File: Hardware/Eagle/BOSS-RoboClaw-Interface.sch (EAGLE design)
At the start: 9 parts, among them IC1 ISO7221ISO7221, J1 MOLEX 22112022, J2 MOLEX 22122034, J3 Amphenol 75869-130LF, J4 SAMTEC ESQ-105-44-G-S, J5 SAMTEC ESW-110-44-S-D, X1 Amphenol L77SDAH15SOL2RM8C309

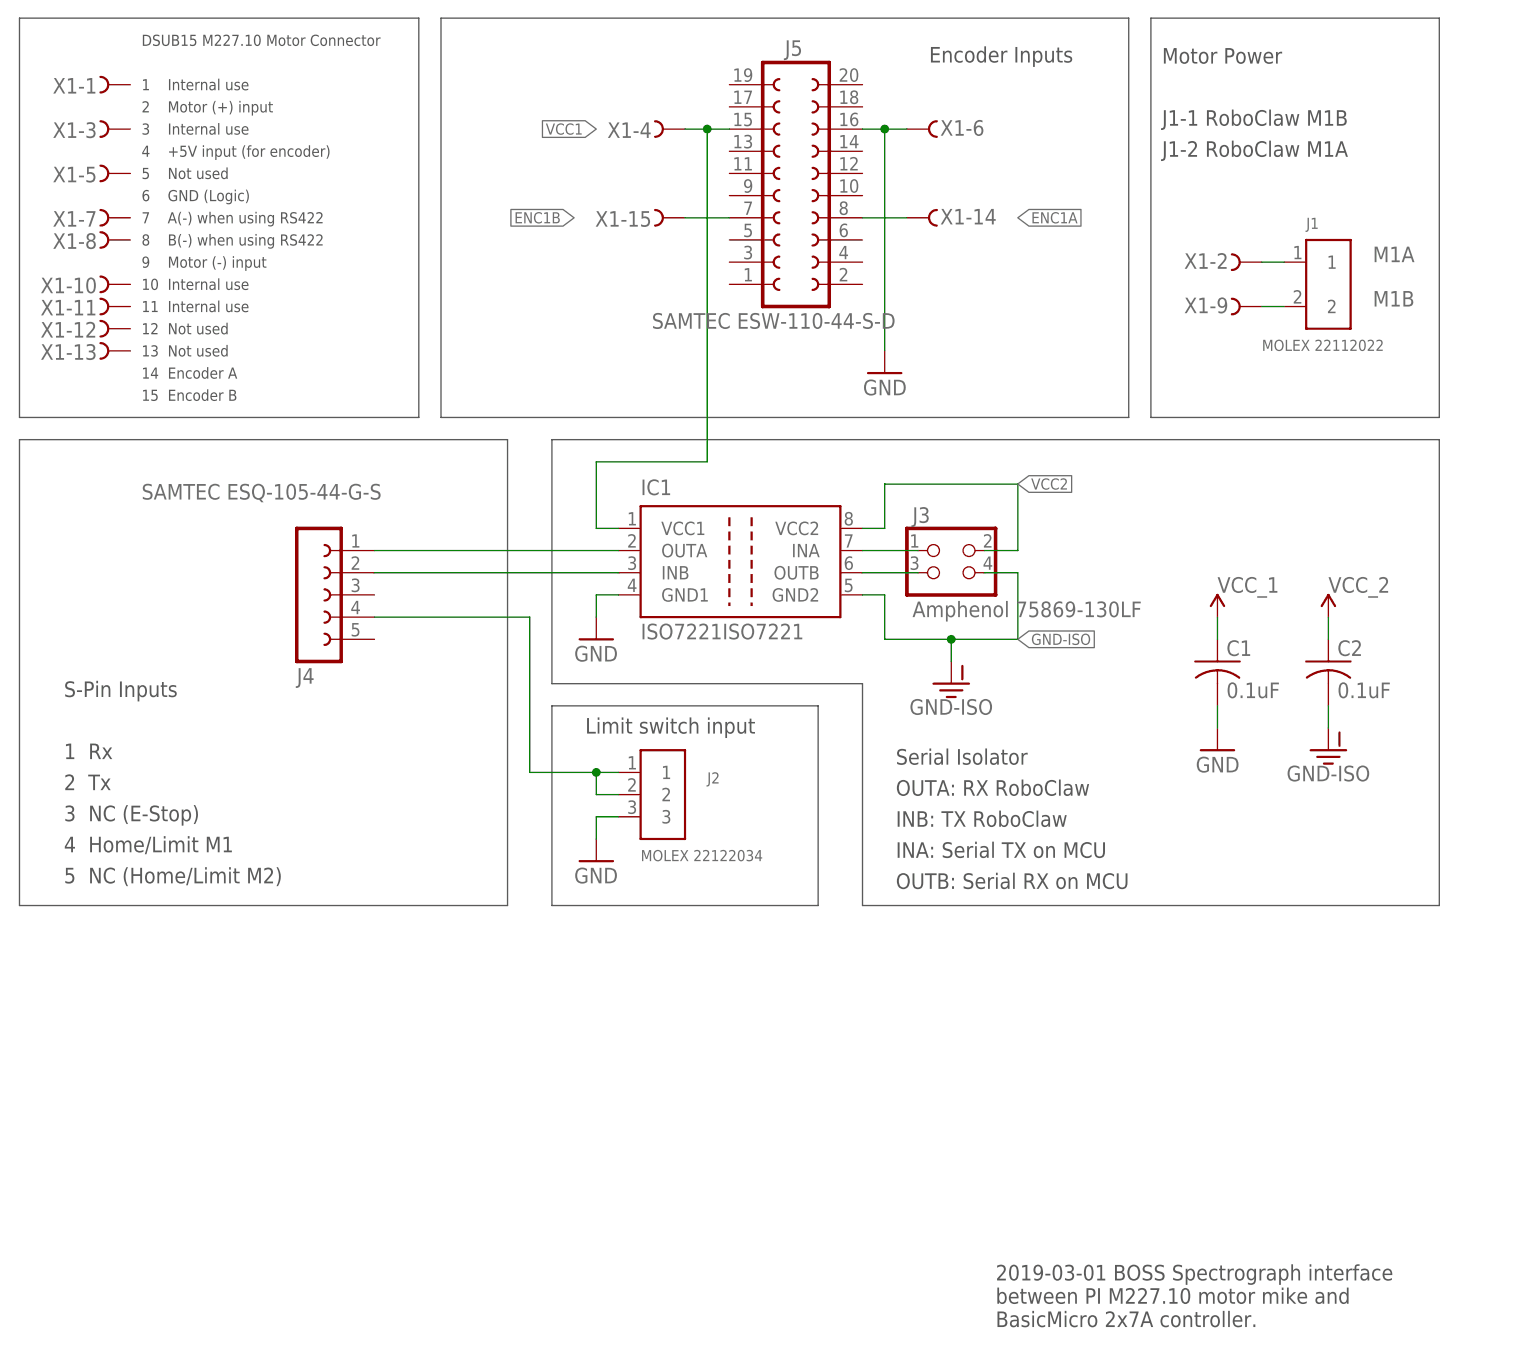
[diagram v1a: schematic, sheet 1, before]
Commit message: New headers for RoboClaw interface (need to check connections)
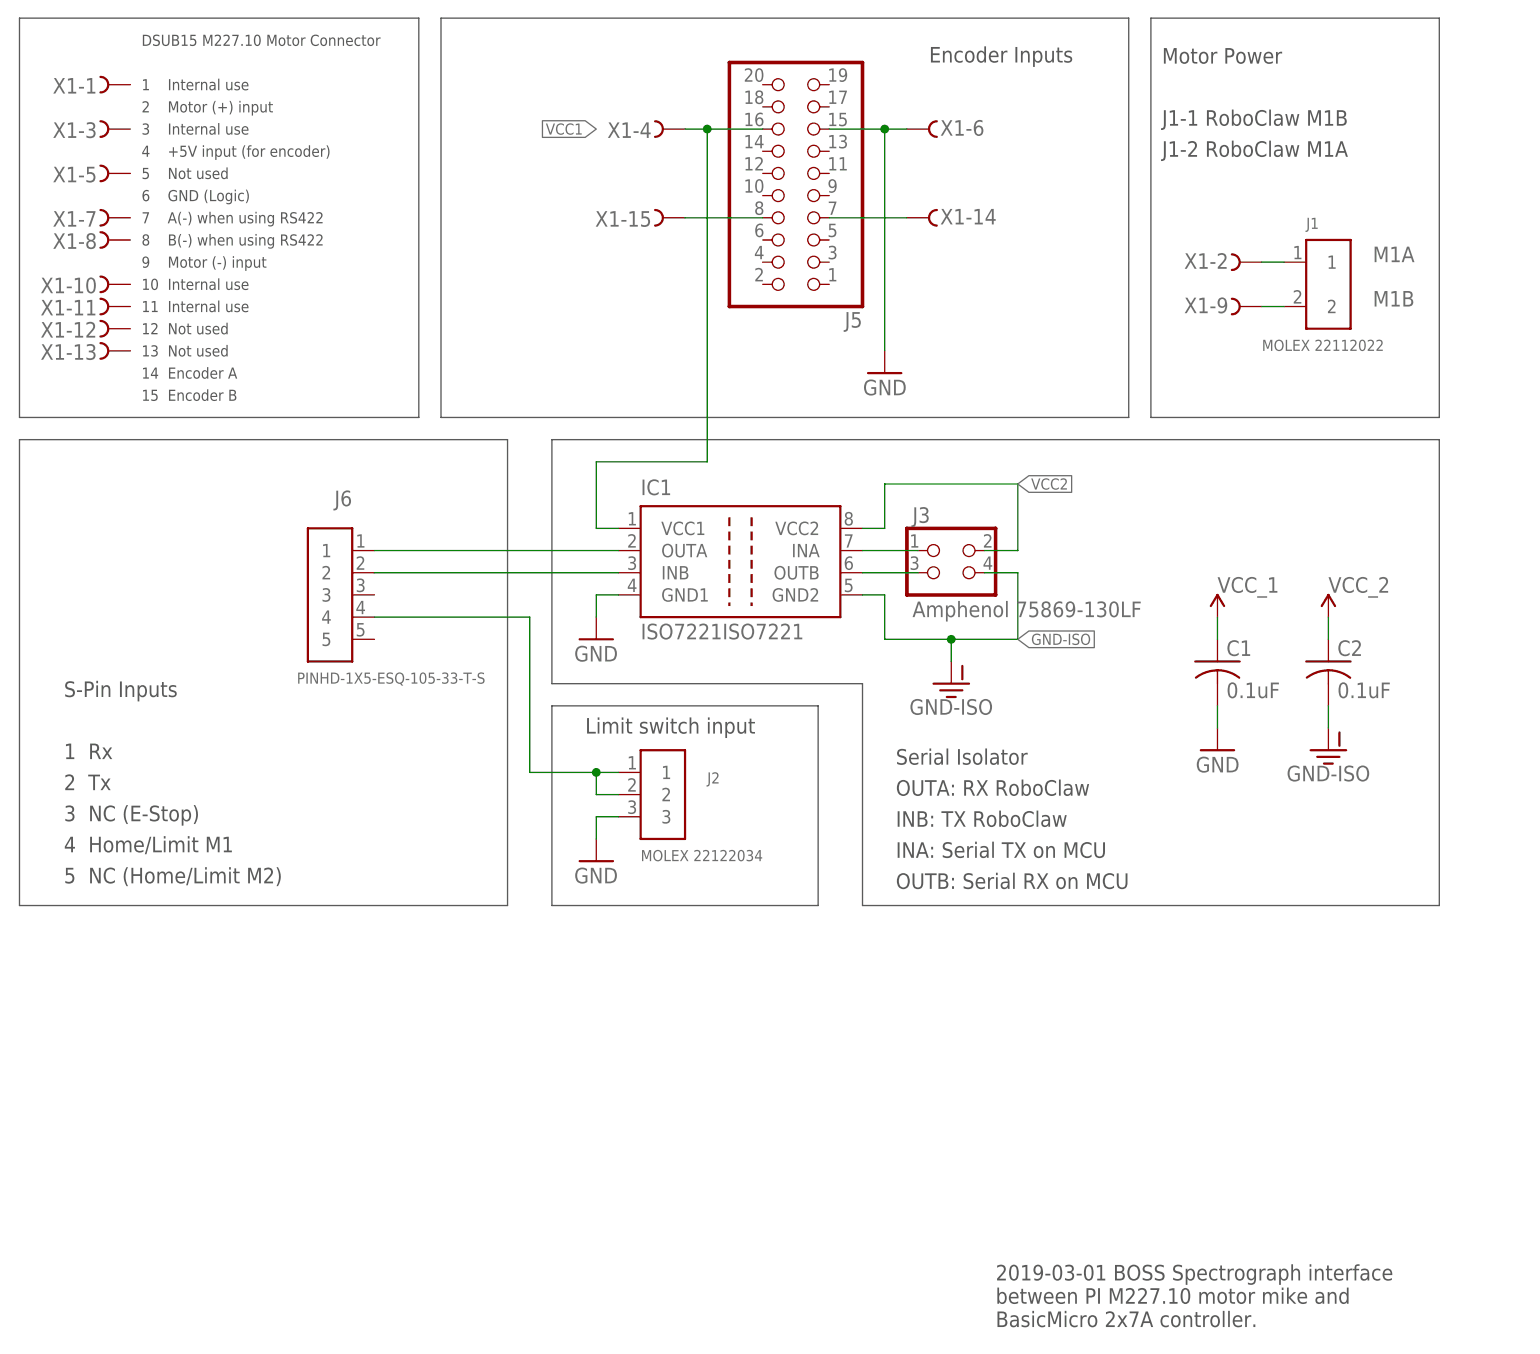
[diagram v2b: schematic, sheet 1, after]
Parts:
- removed J4: SAMTEC ESQ-105-44-G-S, AUmlib:FE05-1
- added J6: PINHD-1X5-ESQ-105-33-T-S, AUmlib:PINHD-1X5-ESQ-105-33-T-S
- J5: value SAMTEC ESW-110-44-S-D -> (none); device AUmlib:FE10-2SAMTEC-ESW-110-44-S-D -> AUmlib:PINHD-2X10-ESQ-110-33-T-DSAMTEC
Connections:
- removed net ENC1A: J5.8, X1-14.F
- removed net ENC1B: J5.7, X1-15.F
- new net N$1: J5.8, X1-15.F
- new net N$2: J5.7, X1-14.F
- net GND: now also J5.15; no longer J5.16
- net LIMIT: now also J6.4; no longer J4.4
- net RX: now also J6.1; no longer J4.1
- net TX: now also J6.2; no longer J4.2
- net VCC1: now also J5.16; no longer J5.15
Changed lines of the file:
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@@
 <setting verticaltext="up"/>
 </settings>
-<grid distance="0.1" unitdist="inch" unit="inch" style="lines" multiple="1" display="no" altdistance="0.01" altunitdist="inch" altunit="inch"/>
+<grid distance="0.05" unitdist="inch" unit="inch" style="lines" multiple="1" display="yes" altdistance="0.01" altunitdist="inch" altunit="inch"/>
 <layers>
 <layer number="1" name="Top" color="4" fill="1" visible="no" active="no"/>
@@
 <part name="IC1" library="AUmlib" library_urn="urn:adsk.eagle:library:9166017" deviceset="ISO7221" device="ISO7221" package3d_urn="urn:adsk.eagle:package:24898359/3"/>
 <part name="J3" library="AUmlib" library_urn="urn:adsk.eagle:library:9166017" deviceset="PINHD-2X2" device="AMP-75869-130LF" package3d_urn="urn:adsk.eagle:package:24897806/2" value="Amphenol 75869-130LF"/>
-<part name="J4" library="AUmlib" library_urn="urn:adsk.eagle:library:9166017" deviceset="FE05-1" device="" package3d_urn="urn:adsk.eagle:package:9166100/8" value="SAMTEC ESQ-105-44-G-S"/>
-<part name="J5" library="AUmlib" library_urn="urn:adsk.eagle:library:9166017" deviceset="FE10-2" device="SAMTEC-ESW-110-44-S-D" package3d_urn="urn:adsk.eagle:package:24899505/2" value="SAMTEC ESW-110-44-S-D"/>
 <part name="J1" library="AUmlib" library_urn="urn:adsk.eagle:library:9166017" deviceset="PINHD-1X2-MOLEX-22112022" device="" package3d_urn="urn:adsk.eagle:package:24727026/5" value="MOLEX 22112022"/>
 <part name="J2" library="AUmlib" library_urn="urn:adsk.eagle:library:9166017" deviceset="PINHD-1X3RA-MOLEX-22122034" device="" package3d_urn="urn:adsk.eagle:package:24728688/10" value="MOLEX 22122034"/>
 <part name="FRAME1" library="frames" library_urn="urn:adsk.eagle:library:229" deviceset="FRAME_A_L" device="" value="Letter Frame"/>
+<part name="J6" library="AUmlib" library_urn="urn:adsk.eagle:library:9166017" deviceset="PINHD-1X5-ESQ-105-33-T-S" device="" package3d_urn="urn:adsk.eagle:package:24929591/4"/>
+<part name="J5" library="AUmlib" library_urn="urn:adsk.eagle:library:9166017" deviceset="PINHD-2X10-ESQ-110-33-T-D" device="SAMTEC" package3d_urn="urn:adsk.eagle:package:24929474/2"/>
 </parts>
 <sheets>
@@
 <attribute name="VALUE" x="170.815" y="106.68" size="1.778" layer="96" ratio="10"/>
 </instance>
-<instance part="J4" gate="G$1" x="101.6" y="109.22" smashed="yes" rot="MR180">
-<attribute name="VALUE" x="82.55" y="121.92" size="1.778" layer="96" ratio="10" rot="MR180"/>
-<attribute name="NAME" x="100.33" y="100.838" size="1.778" layer="95" rot="MR180"/>
-</instance>
-<instance part="J5" gate="G$1" x="157.48" y="154.94" smashed="yes">
-<attribute name="VALUE" x="140.97" y="139.7" size="1.778" layer="96" ratio="10"/>
-<attribute name="NAME" x="156.21" y="170.942" size="1.778" layer="95"/>
-</instance>
 <instance part="J1" gate="G$1" x="218.44" y="144.78" smashed="yes">
 <attribute name="NAME" x="215.9" y="151.13" size="1.27" layer="95"/>
@@
 <attribute name="DRAWING_NAME" x="190.5" y="19.05" size="2.54" layer="94"/>
 </instance>
+<instance part="J6" gate="G$1" x="104.14" y="109.22" smashed="yes" rot="MR0">
+<attribute name="NAME" x="106.68" y="119.38" size="1.778" layer="95" rot="MR0"/>
+<attribute name="VALUE" x="121.92" y="99.06" size="1.27" layer="96" rot="MR0"/>
+</instance>
+<instance part="J5" gate="A" x="158.75" y="154.94" smashed="yes" rot="R180">
+<attribute name="NAME" x="165.1" y="141.605" size="1.778" layer="95" rot="R180"/>
+<attribute name="VALUE" x="165.1" y="172.72" size="1.778" layer="96" rot="R180"/>
+</instance>
 </instances>
 <busses>
@@
 <segment>
 <pinref part="X1" gate="-6" pin="F"/>
-<wire x1="165.1" y1="162.56" x2="167.64" y2="162.56" width="0.1524" layer="91"/>
 <pinref part="GND4" gate="1" pin="GND"/>
 <wire x1="167.64" y1="162.56" x2="170.18" y2="162.56" width="0.1524" layer="91"/>
 <wire x1="167.64" y1="137.16" x2="167.64" y2="162.56" width="0.1524" layer="91"/>
+<pinref part="J5" gate="A" pin="15"/>
+<wire x1="161.29" y1="162.56" x2="167.64" y2="162.56" width="0.1524" layer="91"/>
 <junction x="167.64" y="162.56"/>
-<pinref part="J5" gate="G$1" pin="16"/>
 </segment>
 </net>
@@
 <wire x1="109.22" y1="114.3" x2="137.16" y2="114.3" width="0.1524" layer="91"/>
 <pinref part="IC1" gate="G$1" pin="OUTA"/>
-<pinref part="J4" gate="G$1" pin="1"/>
+<pinref part="J6" gate="G$1" pin="1"/>
 </segment>
 </net>
@@
 <wire x1="109.22" y1="111.76" x2="137.16" y2="111.76" width="0.1524" layer="91"/>
 <pinref part="IC1" gate="G$1" pin="INB"/>
-<pinref part="J4" gate="G$1" pin="2"/>
+<pinref part="J6" gate="G$1" pin="2"/>
 </segment>
 </net>
@@
 <wire x1="127" y1="88.9" x2="134.62" y2="88.9" width="0.1524" layer="91"/>
 <wire x1="134.62" y1="86.36" x2="134.62" y2="88.9" width="0.1524" layer="91"/>
-<pinref part="J4" gate="G$1" pin="4"/>
 <pinref part="J2" gate="G$1" pin="1"/>
 <wire x1="134.62" y1="88.9" x2="137.16" y2="88.9" width="0.1524" layer="91"/>
@@
 <pinref part="J2" gate="G$1" pin="2"/>
 <wire x1="134.62" y1="86.36" x2="137.16" y2="86.36" width="0.1524" layer="91"/>
+<pinref part="J6" gate="G$1" pin="4"/>
 </segment>
 </net>
@@
 <label x="134.62" y="162.56" size="1.27" layer="95" rot="R180" xref="yes"/>
 <wire x1="147.32" y1="124.46" x2="147.32" y2="162.56" width="0.1524" layer="91"/>
-<wire x1="147.32" y1="162.56" x2="149.86" y2="162.56" width="0.1524" layer="91"/>
 <pinref part="X1" gate="-4" pin="F"/>
 <wire x1="144.78" y1="162.56" x2="147.32" y2="162.56" width="0.1524" layer="91"/>
+<pinref part="IC1" gate="G$1" pin="VCC1"/>
+<pinref part="J5" gate="A" pin="16"/>
+<wire x1="147.32" y1="162.56" x2="153.67" y2="162.56" width="0.1524" layer="91"/>
 <junction x="147.32" y="162.56"/>
-<pinref part="IC1" gate="G$1" pin="VCC1"/>
-<pinref part="J5" gate="G$1" pin="15"/>
 </segment>
 <segment>
@@
 </segment>
 </net>
-<net name="ENC1A" class="0">
-<segment>
-<pinref part="J5" gate="G$1" pin="8"/>
+<net name="N$1" class="0">
+<segment>
+<pinref part="X1" gate="-15" pin="F"/>
+<pinref part="J5" gate="A" pin="8"/>
+<wire x1="144.78" y1="152.4" x2="153.67" y2="152.4" width="0.1524" layer="91"/>
+</segment>
+</net>
+<net name="N$2" class="0">
+<segment>
+<pinref part="J5" gate="A" pin="7"/>
 <pinref part="X1" gate="-14" pin="F"/>
-<wire x1="165.1" y1="152.4" x2="170.18" y2="152.4" width="0.1524" layer="91"/>
-<label x="182.88" y="152.4" size="1.27" layer="95" xref="yes"/>
-</segment>
-</net>
-<net name="ENC1B" class="0">
-<segment>
-<pinref part="J5" gate="G$1" pin="7"/>
-<pinref part="X1" gate="-15" pin="F"/>
-<wire x1="149.86" y1="152.4" x2="144.78" y2="152.4" width="0.1524" layer="91"/>
-<label x="132.08" y="152.4" size="1.27" layer="95" rot="R180" xref="yes"/>
-</segment>
-</net>
+<wire x1="161.29" y1="152.4" x2="170.18" y2="152.4" width="0.1524" layer="91"/>
+</segment>
+</net>

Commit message: Swapped ENC-A and ENC-B pins to be consistent
Also updated the board labels and changed the date to 2020-11-23.
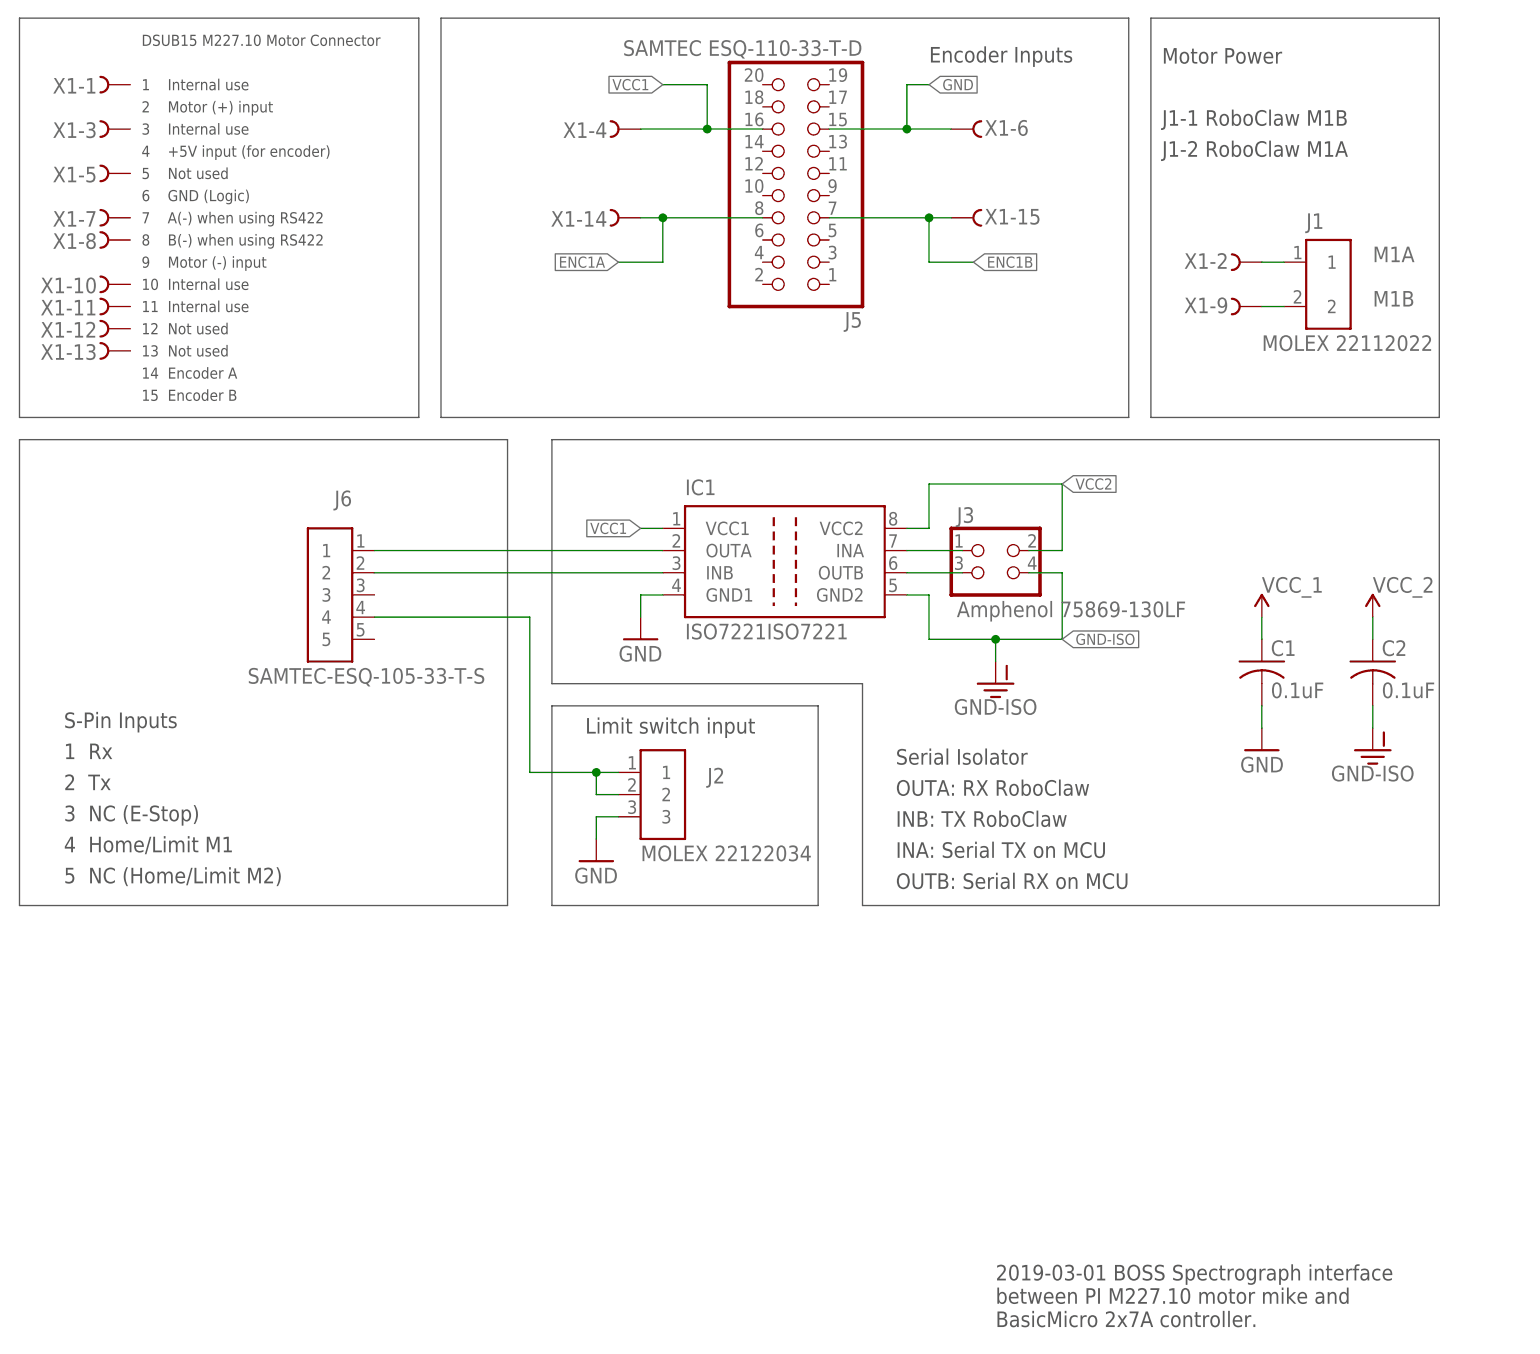
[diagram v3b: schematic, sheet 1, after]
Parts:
- J5: value (none) -> SAMTEC ESQ-110-33-T-D
- J6: value PINHD-1X5-ESQ-105-33-T-S -> SAMTEC-ESQ-105-33-T-S
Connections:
- removed net N$1: J5.8, X1-15.F
- removed net N$2: J5.7, X1-14.F
- new net ENC1A: J5.8, X1-14.F
- new net ENC1B: J5.7, X1-15.F
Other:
- moved on the sheet: C1, C2, IC1, J3, X1-14, X1-15, X1-4, X1-6

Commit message: No changes made; just saved new version
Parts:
- IC1: value ISO7221ISO7221 -> TI ISO7221ADR
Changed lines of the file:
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@@
 <setting verticaltext="up"/>
 </settings>
-<grid distance="0.1" unitdist="inch" unit="inch" style="lines" multiple="1" display="yes" altdistance="0.01" altunitdist="inch" altunit="inch"/>
+<grid distance="0.1" unitdist="inch" unit="inch" style="lines" multiple="1" display="no" altdistance="0.01" altunitdist="inch" altunit="inch"/>
 <layers>
 <layer number="1" name="Top" color="4" fill="1" visible="no" active="no"/>
@@
 <part name="GND-ISO1" library="AUmlib" library_urn="urn:adsk.eagle:library:9166017" deviceset="GND-ISO" device=""/>
 <part name="GND-ISO2" library="AUmlib" library_urn="urn:adsk.eagle:library:9166017" deviceset="GND-ISO" device=""/>
-<part name="IC1" library="AUmlib" library_urn="urn:adsk.eagle:library:9166017" deviceset="ISO7221" device="ISO7221" package3d_urn="urn:adsk.eagle:package:24898359/3"/>
+<part name="IC1" library="AUmlib" library_urn="urn:adsk.eagle:library:9166017" deviceset="ISO7221" device="ISO7221" package3d_urn="urn:adsk.eagle:package:24898359/3" value="TI ISO7221ADR"/>
 <part name="J3" library="AUmlib" library_urn="urn:adsk.eagle:library:9166017" deviceset="PINHD-2X2" device="AMP-75869-130LF" package3d_urn="urn:adsk.eagle:package:24897806/2" value="Amphenol 75869-130LF"/>
 <part name="J1" library="AUmlib" library_urn="urn:adsk.eagle:library:9166017" deviceset="PINHD-1X2-MOLEX-22112022" device="" package3d_urn="urn:adsk.eagle:package:24727026/5" value="MOLEX 22112022"/>
